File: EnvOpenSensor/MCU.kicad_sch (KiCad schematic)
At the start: 33 parts, among them J2 SM03B-SRSS-TB, SW5 B3U-1000, SW6 B3U-1000, U4 W25Q16JVUXIQ, U5 RP2350_60QFN, Y1 ABM8-272-T3

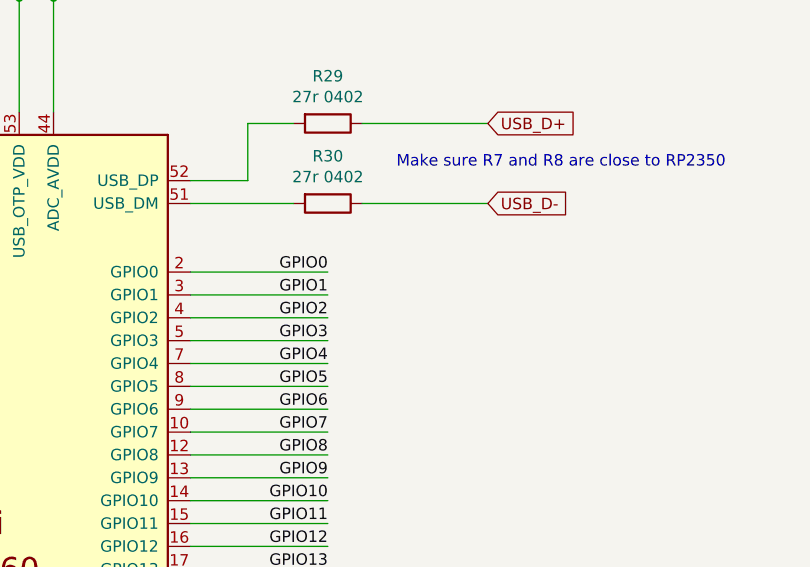
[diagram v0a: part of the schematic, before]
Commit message: finished routing up board, needs a double-check
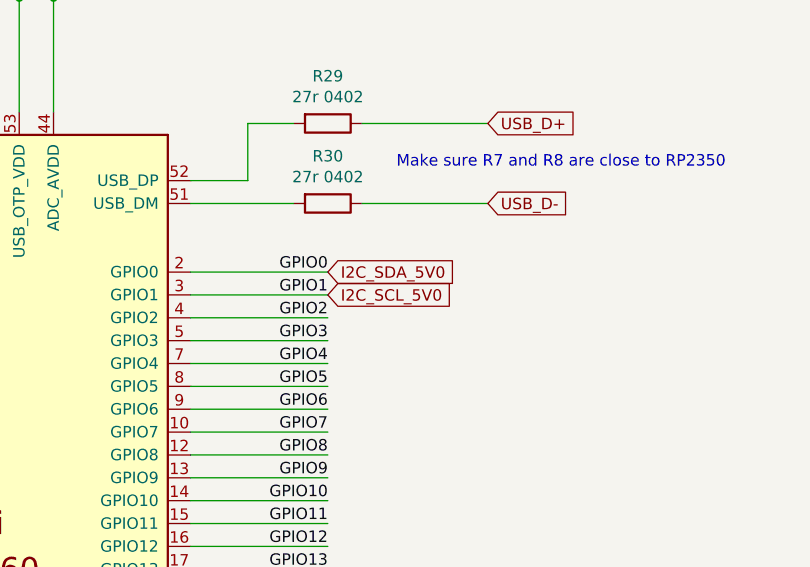
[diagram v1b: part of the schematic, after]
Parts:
- C31, C32: footprint Capacitor_SMD:C_0402_1005Metric -> RP2350_60QFN_minimal:C_0402_1005Metric_small_pads
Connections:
- net GPIO0 renamed I2C_SDA_5V0
- net GPIO1 renamed I2C_SCL_5V0
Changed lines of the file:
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@@
+		)
+	)
+	(global_label "I2C_SCL_5V0"
+		(shape input)
+		(at 207.645 78.105 0)
+		(fields_autoplaced yes)
+		(effects
+			(font
+				(size 1.27 1.27)
+			)
+			(justify left)
+		)
+		(property "Intersheetrefs" "${INTERSHEET_REFS}"
+			(at 222.6649 78.105 0)
+			(effects
+				(font
+					(size 1.27 1.27)
+				)
+				(justify left)
+				(hide yes)
+			)
+		)
+	)
+	(global_label "I2C_SDA_5V0"
+		(shape input)
+		(at 207.645 75.565 0)
+		(fields_autoplaced yes)
+		(effects
+			(font
+				(size 1.27 1.27)
+			)
+			(justify left)
+		)
+		(property "Intersheetrefs" "${INTERSHEET_REFS}"
+			(at 222.7254 75.565 0)
+			(effects
+				(font
+					(size 1.27 1.27)
+				)
+				(justify left)
+				(hide yes)
+			)
 		)
 	)
@@
 			)
 		)
-		(property "Footprint" "Capacitor_SMD:C_0402_1005Metric"
+		(property "Footprint" "RP2350_60QFN_minimal:C_0402_1005Metric_small_pads"
 			(at 71.4502 75.565 0)
 			(effects
@@
 			)
 		)
-		(property "Footprint" "Capacitor_SMD:C_0402_1005Metric"
+		(property "Footprint" "RP2350_60QFN_minimal:C_0402_1005Metric_small_pads"
 			(at 82.8802 75.565 0)
 			(effects

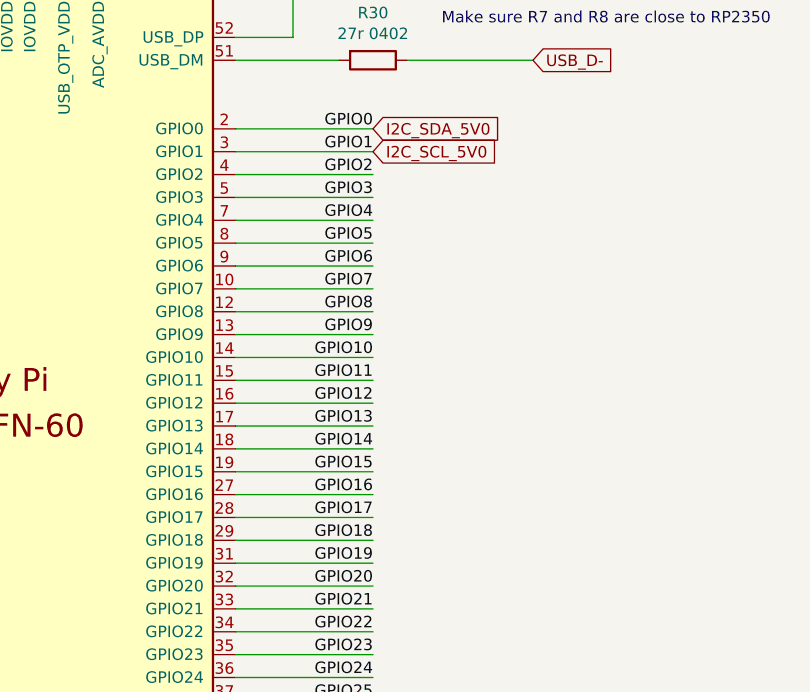
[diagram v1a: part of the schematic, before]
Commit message: moved reset button - easier to access, added button labels, wired up switches
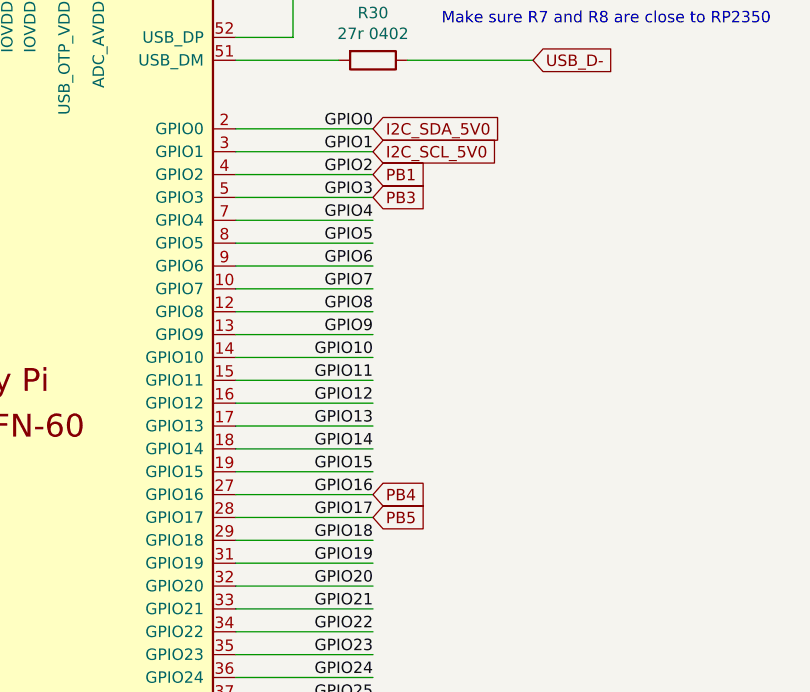
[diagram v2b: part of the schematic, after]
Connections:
- net GPIO16 renamed PB4
- net GPIO17 renamed PB5
- net GPIO2 renamed PB1
- net GPIO3 renamed PB3
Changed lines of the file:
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@@
+		)
+	)
+	(global_label "PB3"
+		(shape input)
+		(at 207.645 83.185 0)
+		(fields_autoplaced yes)
+		(effects
+			(font
+				(size 1.27 1.27)
+			)
+			(justify left)
+		)
+		(property "Intersheetrefs" "${INTERSHEET_REFS}"
+			(at 214.3797 83.185 0)
+			(effects
+				(font
+					(size 1.27 1.27)
+				)
+				(justify left)
+				(hide yes)
+			)
+		)
+	)
+	(global_label "PB5"
+		(shape input)
+		(at 207.645 118.745 0)
+		(fields_autoplaced yes)
+		(effects
+			(font
+				(size 1.27 1.27)
+			)
+			(justify left)
+		)
+		(property "Intersheetrefs" "${INTERSHEET_REFS}"
+			(at 214.3797 118.745 0)
+			(effects
+				(font
+					(size 1.27 1.27)
+				)
+				(justify left)
+				(hide yes)
+			)
 		)
 	)
@@
 		)
 	)
+	(global_label "PB1"
+		(shape input)
+		(at 207.645 80.645 0)
+		(fields_autoplaced yes)
+		(effects
+			(font
+				(size 1.27 1.27)
+			)
+			(justify left)
+		)
+		(property "Intersheetrefs" "${INTERSHEET_REFS}"
+			(at 214.3797 80.645 0)
+			(effects
+				(font
+					(size 1.27 1.27)
+				)
+				(justify left)
+				(hide yes)
+			)
+		)
+	)
 	(global_label "I2C_SDA_5V0"
 		(shape input)
@@
 			(effects
 				(font
+					(size 1.27 1.27)
+				)
+				(justify left)
+				(hide yes)
+			)
+		)
+	)
+	(global_label "PB4"
+		(shape input)
+		(at 207.645 116.205 0)
+		(fields_autoplaced yes)
+		(effects
+			(font
+				(size 1.27 1.27)
+			)
+			(justify left)
+		)
+		(property "Intersheetrefs" "${INTERSHEET_REFS}"
+			(at 214.3797 116.205 0)
+			(effects
+				(font

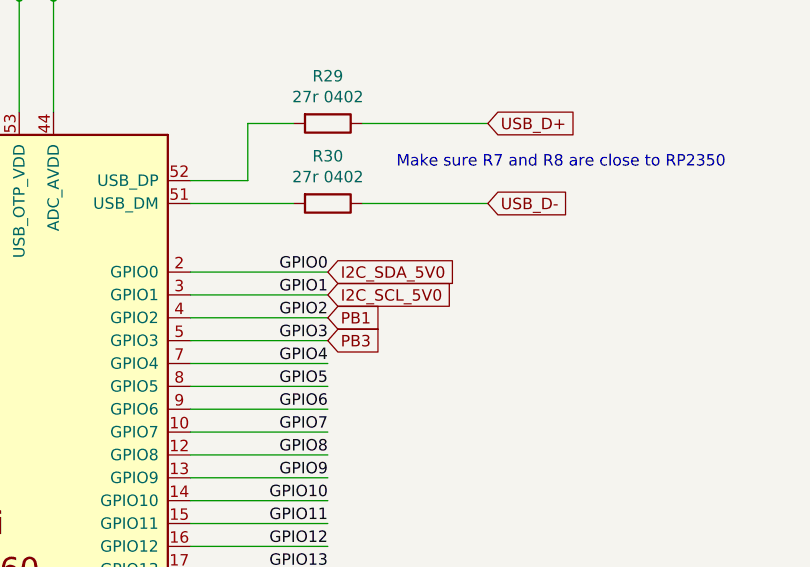
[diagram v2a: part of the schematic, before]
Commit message: Added level shifter IC and fixed incorrect wiring + label
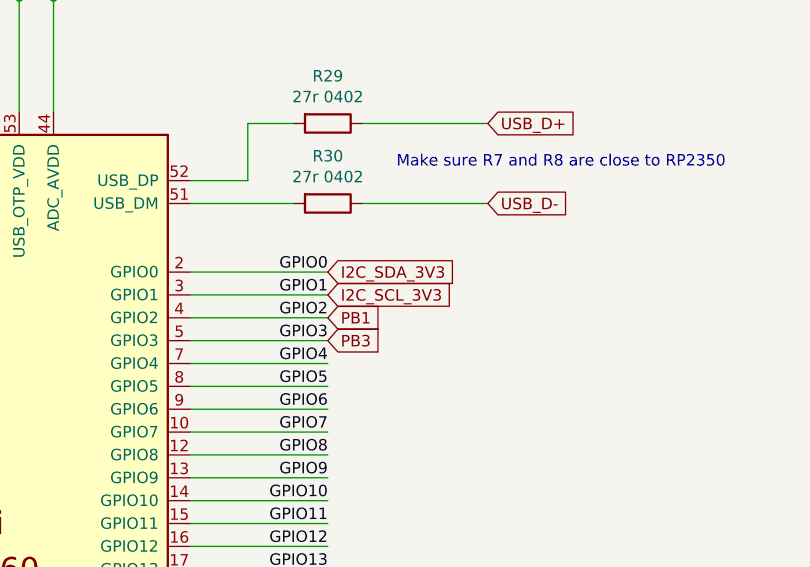
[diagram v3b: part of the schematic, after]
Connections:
- net I2C_SCL_5V0 renamed I2C_SCL_3V3
- net I2C_SDA_5V0 renamed I2C_SDA_3V3
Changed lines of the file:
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@@
+		)
+	)
+	(global_label "I2C_SCL_3V3"
+		(shape input)
+		(at 207.645 78.105 0)
+		(fields_autoplaced yes)
+		(effects
+			(font
+				(size 1.27 1.27)
+			)
+			(justify left)
+		)
+		(property "Intersheetrefs" "${INTERSHEET_REFS}"
+			(at 222.6649 78.105 0)
+			(effects
+				(font
+					(size 1.27 1.27)
+				)
+				(justify left)
+				(hide yes)
+			)
 		)
 	)
@@
 		)
 	)
-	(global_label "I2C_SCL_5V0"
-		(shape input)
-		(at 207.645 78.105 0)
-		(fields_autoplaced yes)
-		(effects
-			(font
-				(size 1.27 1.27)
-			)
-			(justify left)
-		)
-		(property "Intersheetrefs" "${INTERSHEET_REFS}"
-			(at 222.6649 78.105 0)
-			(effects
-				(font
-					(size 1.27 1.27)
-				)
-				(justify left)
-				(hide yes)
-			)
-		)
-	)
 	(global_label "PB1"
 		(shape input)
@@
 		(property "Intersheetrefs" "${INTERSHEET_REFS}"
 			(at 214.3797 80.645 0)
-			(effects
-				(font
-					(size 1.27 1.27)
-				)
-				(justify left)
-				(hide yes)
-			)
-		)
-	)
-	(global_label "I2C_SDA_5V0"
-		(shape input)
-		(at 207.645 75.565 0)
-		(fields_autoplaced yes)
-		(effects
-			(font
-				(size 1.27 1.27)
-			)
-			(justify left)
-		)
-		(property "Intersheetrefs" "${INTERSHEET_REFS}"
-			(at 222.7254 75.565 0)
 			(effects
 				(font
@@
 			(effects
 				(font
+					(size 1.27 1.27)
+				)
+				(justify left)
+				(hide yes)
+			)
+		)
+	)
+	(global_label "I2C_SDA_3V3"
+		(shape input)
+		(at 207.645 75.565 0)
+		(fields_autoplaced yes)
+		(effects
+			(font
+				(size 1.27 1.27)
+			)
+			(justify left)
+		)
+		(property "Intersheetrefs" "${INTERSHEET_REFS}"
+			(at 222.7254 75.565 0)
+			(effects
+				(font
